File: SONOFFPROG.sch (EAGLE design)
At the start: 3 parts, among them SW1 SWITCH-SPDTB

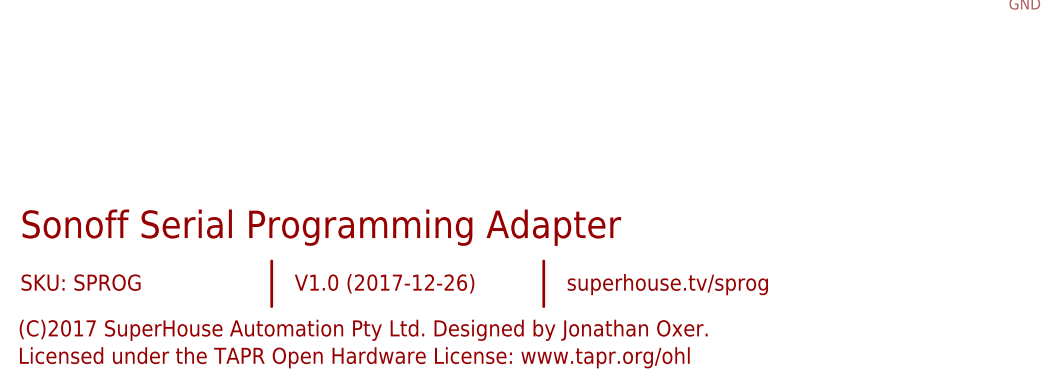
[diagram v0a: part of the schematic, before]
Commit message: Fixed URLs
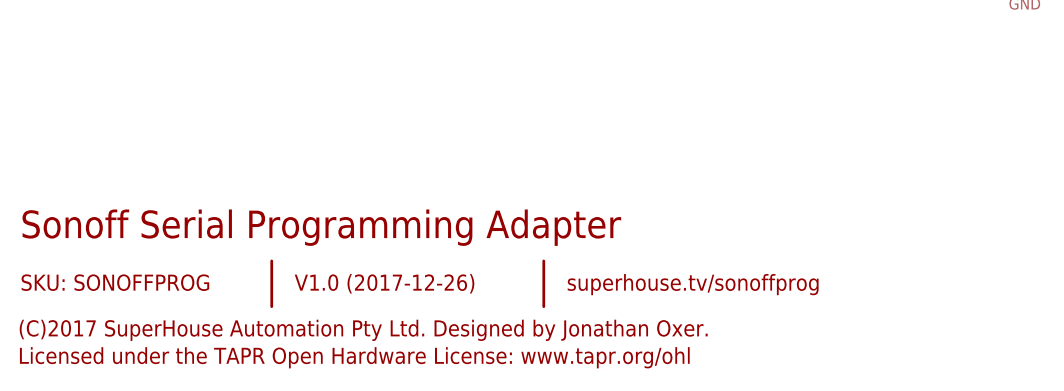
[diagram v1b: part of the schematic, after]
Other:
- note added: "SKU: SONOFFPROG"
- note added: "superhouse.tv/sonoffprog"
- note removed: "SKU: SPROG"
- note removed: "superhouse.tv/sprog"
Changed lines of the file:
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@@
 <?xml version="1.0" encoding="utf-8"?>
 <!DOCTYPE eagle SYSTEM "eagle.dtd">
-<eagle version="8.6.2">
+<eagle version="9.0.1">
 <drawing>
 <settings>
@@
 <text x="7.62" y="20.32" size="3.048" layer="94">Sonoff Serial Programming Adapter</text>
 <text x="38.1" y="14.478" size="1.778" layer="94">V1.0 (2017-12-26)</text>
-<text x="7.62" y="14.478" size="1.778" layer="94">SKU: SPROG</text>
+<text x="7.62" y="14.478" size="1.778" layer="94">SKU: SONOFFPROG</text>
 <text x="7.366" y="9.398" size="1.778" layer="94">(C)2017 SuperHouse Automation Pty Ltd. Designed by Jonathan Oxer.</text>
 <text x="7.366" y="6.35" size="1.778" layer="94">Licensed under the TAPR Open Hardware License: www.tapr.org/ohl</text>
-<text x="68.326" y="14.478" size="1.778" layer="94">superhouse.tv/sprog</text>
+<text x="68.326" y="14.478" size="1.778" layer="94">superhouse.tv/sonoffprog</text>
 <frame x1="0" y1="0" x2="190.5" y2="127" columns="8" rows="5" layer="94"/>
 <frame x1="5.08" y1="12.7" x2="109.22" y2="25.4" columns="0" rows="0" layer="94" border-left="no" border-top="no" border-right="no" border-bottom="no"/>

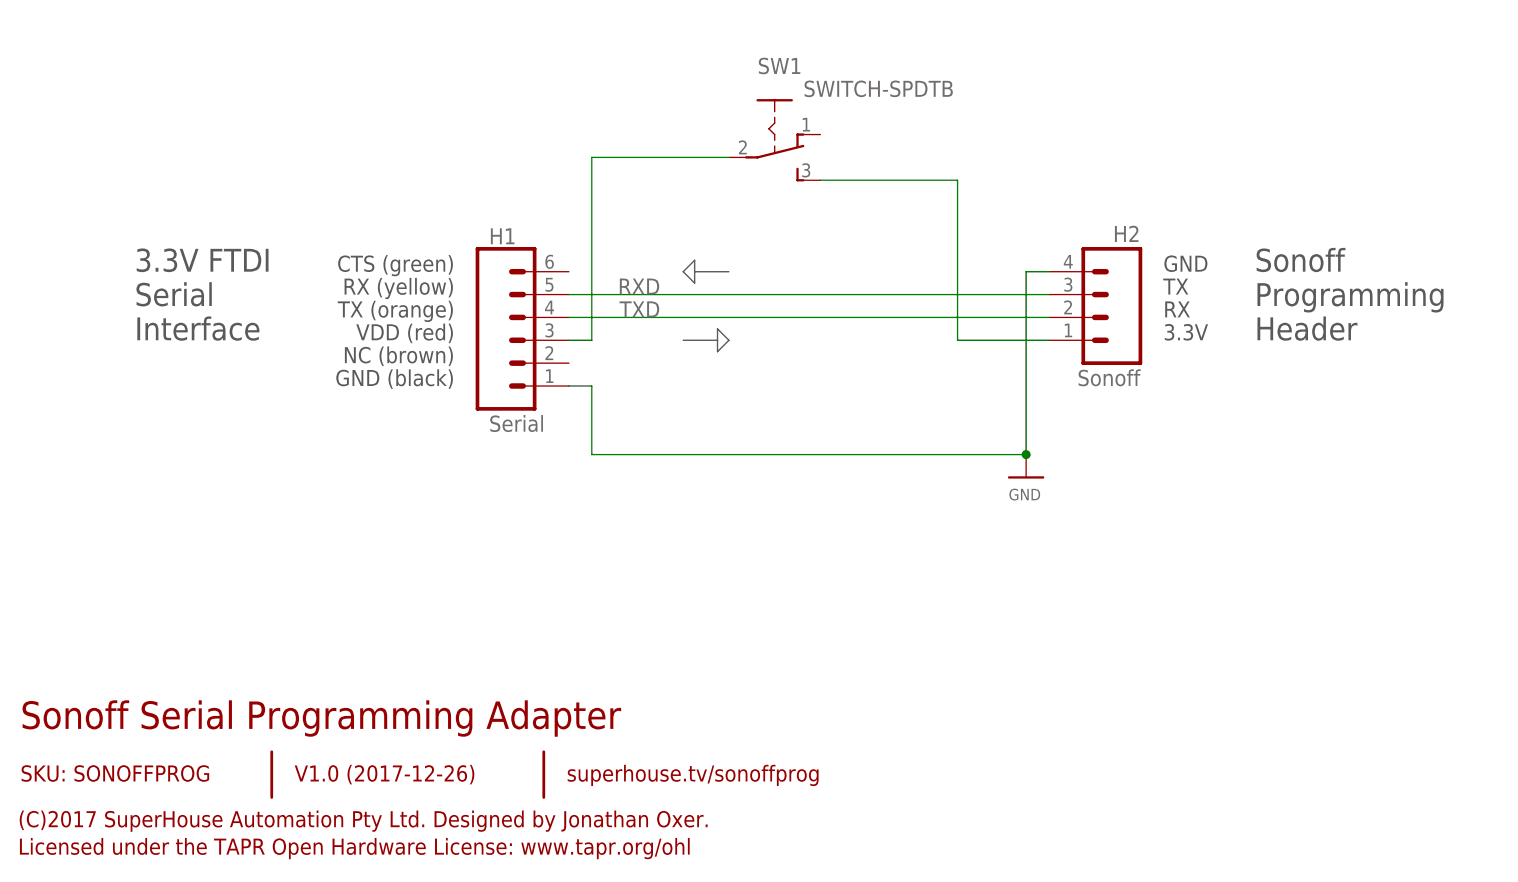
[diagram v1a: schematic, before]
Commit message: Replaced jumper with NC button, and added GND header for v2.0 release
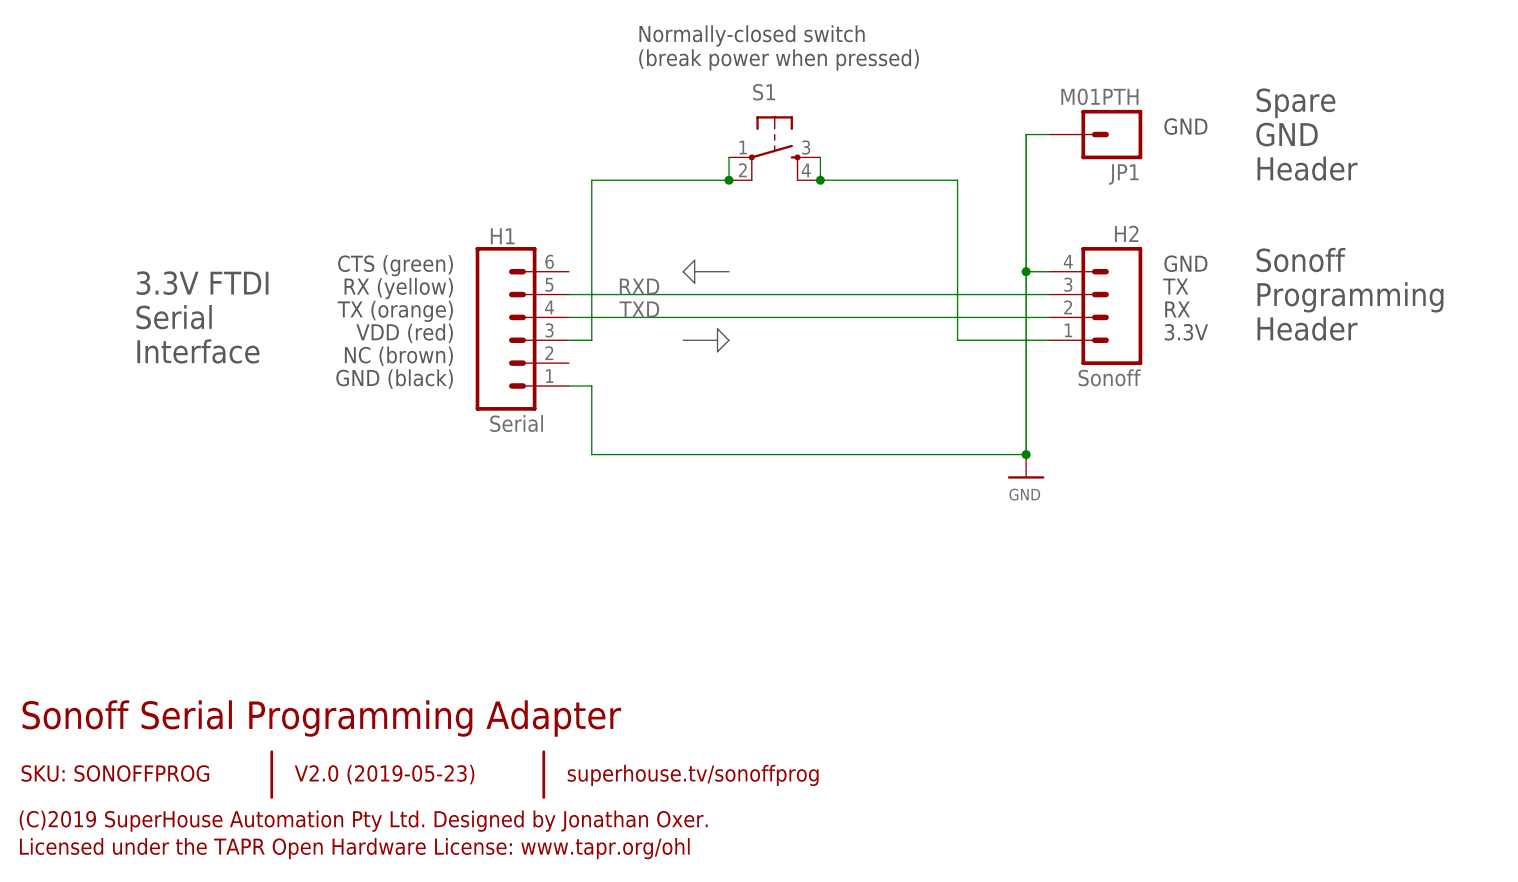
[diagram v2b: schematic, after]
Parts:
- removed SW1: SWITCH-SPDTB, freetronics-jon:SWITCH-SPDTB
- added JP1: M01PTH, freetronics-original:M01PTH
- added S1: (no value), freetronics-original:TAC_SWITCHPTH
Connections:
- net GND: now also JP1.1
- net N$1: now also S1.3, S1.4; no longer SW1.3
- net N$4: now also S1.1, S1.2; no longer SW1.2
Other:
- note added: "(C)2019 SuperHouse Automation Pty Ltd. Designed by Jonathan Oxer."
- note added: "Normally-closed switch (break power when pressed)"
- note added: "Spare GND Header"
- note added: "V2.0 (2019-05-23)"
- note removed: "(C)2017 SuperHouse Automation Pty Ltd. Designed by Jonathan Oxer."
- note removed: "V1.0 (2017-12-26)"
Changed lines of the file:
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@@
 <?xml version="1.0" encoding="utf-8"?>
 <!DOCTYPE eagle SYSTEM "eagle.dtd">
-<eagle version="9.0.1">
+<eagle version="9.4.0">
 <drawing>
 <settings>
@@
 <setting verticaltext="up"/>
 </settings>
-<grid distance="0.05" unitdist="inch" unit="inch" style="lines" multiple="1" display="no" altdistance="0.01" altunitdist="inch" altunit="inch"/>
+<grid distance="0.1" unitdist="inch" unit="inch" style="lines" multiple="1" display="no" altdistance="0.01" altunitdist="inch" altunit="inch"/>
 <layers>
 <layer number="1" name="Top" color="4" fill="1" visible="no" active="no"/>
@@
 <part name="U$21" library="freetronics-luke" deviceset="GND" device=""/>
 <part name="H2" library="freetronics-jon" deviceset="M04" device="PTH" value="Sonoff"/>
-<part name="SW1" library="freetronics-jon" deviceset="SWITCH-SPDT" device="B" value="SWITCH-SPDTB"/>
+<part name="S1" library="freetronics-original" deviceset="TAC_SWITCH" device="PTH"/>
+<part name="JP1" library="freetronics-original" deviceset="M01" device="PTH"/>
 </parts>
 <sheets>
@@
 <wire x1="65.786" y1="17.78" x2="65.786" y2="12.7" width="0.3048" layer="94"/>
 <text x="7.62" y="20.32" size="3.048" layer="94">Sonoff Serial Programming Adapter</text>
-<text x="38.1" y="14.478" size="1.778" layer="94">V1.0 (2017-12-26)</text>
+<text x="38.1" y="14.478" size="1.778" layer="94">V2.0 (2019-05-23)</text>
 <text x="7.62" y="14.478" size="1.778" layer="94">SKU: SONOFFPROG</text>
-<text x="7.366" y="9.398" size="1.778" layer="94">(C)2017 SuperHouse Automation Pty Ltd. Designed by Jonathan Oxer.</text>
+<text x="7.366" y="9.398" size="1.778" layer="94">(C)2019 SuperHouse Automation Pty Ltd. Designed by Jonathan Oxer.</text>
 <text x="7.366" y="6.35" size="1.778" layer="94">Licensed under the TAPR Open Hardware License: www.tapr.org/ohl</text>
 <text x="68.326" y="14.478" size="1.778" layer="94">superhouse.tv/sonoffprog</text>
@@
 <text x="134.62" y="68.58" size="1.778" layer="97">TX</text>
 <text x="134.62" y="71.12" size="1.778" layer="97">GND</text>
-<text x="20.32" y="63.5" size="2.54" layer="97">3.3V FTDI
+<text x="20.32" y="60.96" size="2.54" layer="97">3.3V FTDI
 Serial
 Interface</text>
@@
 <wire x1="85.09" y1="63.5" x2="81.28" y2="63.5" width="0.1524" layer="97"/>
 <wire x1="82.55" y1="71.12" x2="86.36" y2="71.12" width="0.1524" layer="97"/>
+<text x="134.62" y="86.36" size="1.778" layer="97">GND</text>
+<text x="144.78" y="81.28" size="2.54" layer="97">Spare
+GND
+Header</text>
+<text x="76.2" y="93.98" size="1.778" layer="97">Normally-closed switch
+(break power when pressed)</text>
 </plain>
 <instances>
@@
 <attribute name="VALUE" x="59.69" y="55.118" size="1.778" layer="96" rot="MR180"/>
 </instance>
-<instance part="U$21" gate="G$1" x="119.38" y="48.26" rot="MR0"/>
-<instance part="H2" gate="G$1" x="127" y="66.04" rot="MR0"/>
-<instance part="SW1" gate="G$1" x="91.44" y="86.36" rot="R270"/>
+<instance part="U$21" gate="G$1" x="119.38" y="48.26" smashed="yes" rot="MR0">
+<attribute name="VALUE" x="121.031" y="45.72" size="1.27" layer="96" rot="MR0"/>
+</instance>
+<instance part="H2" gate="G$1" x="127" y="66.04" smashed="yes" rot="MR0">
+<attribute name="VALUE" x="132.08" y="58.42" size="1.778" layer="96" rot="MR0"/>
+<attribute name="NAME" x="132.08" y="74.422" size="1.778" layer="95" rot="MR0"/>
+</instance>
+<instance part="S1" gate="S" x="91.44" y="83.82" smashed="yes">
+<attribute name="NAME" x="88.9" y="90.17" size="1.778" layer="95"/>
+<attribute name="VALUE" x="88.9" y="77.47" size="1.778" layer="96"/>
+</instance>
+<instance part="JP1" gate="G$1" x="129.54" y="86.36" smashed="yes" rot="R180">
+<attribute name="VALUE" x="132.08" y="91.44" size="1.778" layer="96" rot="R180"/>
+<attribute name="NAME" x="132.08" y="83.058" size="1.778" layer="95" rot="R180"/>
+</instance>
 </instances>
 <busses>
@@
 <wire x1="119.38" y1="71.12" x2="119.38" y2="50.8" width="0.1524" layer="91"/>
 <junction x="119.38" y="50.8"/>
+<pinref part="JP1" gate="G$1" pin="1"/>
+<wire x1="121.92" y1="86.36" x2="119.38" y2="86.36" width="0.1524" layer="91"/>
+<wire x1="119.38" y1="86.36" x2="119.38" y2="71.12" width="0.1524" layer="91"/>
+<junction x="119.38" y="71.12"/>
 </segment>
 </net>
@@
 <wire x1="111.76" y1="63.5" x2="111.76" y2="81.28" width="0.1524" layer="91"/>
 <wire x1="111.76" y1="81.28" x2="96.52" y2="81.28" width="0.1524" layer="91"/>
-<pinref part="SW1" gate="G$1" pin="3"/>
+<pinref part="S1" gate="S" pin="4"/>
+<pinref part="S1" gate="S" pin="3"/>
+<wire x1="96.52" y1="83.82" x2="96.52" y2="81.28" width="0.1524" layer="91"/>
+<junction x="96.52" y="81.28"/>
 </segment>
 </net>
@@
 <wire x1="68.58" y1="63.5" x2="71.12" y2="63.5" width="0.1524" layer="91"/>
 <pinref part="H1" gate="G$1" pin="3"/>
-<wire x1="71.12" y1="83.82" x2="71.12" y2="63.5" width="0.1524" layer="91"/>
-<wire x1="71.12" y1="83.82" x2="86.36" y2="83.82" width="0.1524" layer="91"/>
-<pinref part="SW1" gate="G$1" pin="2"/>
-</segment>
-</net>
+<wire x1="71.12" y1="81.28" x2="71.12" y2="63.5" width="0.1524" layer="91"/>
+<wire x1="71.12" y1="81.28" x2="86.36" y2="81.28" width="0.1524" layer="91"/>
+<pinref part="S1" gate="S" pin="2"/>
+<pinref part="S1" gate="S" pin="1"/>
+<wire x1="86.36" y1="83.82" x2="86.36" y2="81.28" width="0.1524" layer="91"/>
+<junction x="86.36" y="81.28"/>
+</segment>
+</net>
